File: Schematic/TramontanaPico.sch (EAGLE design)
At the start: 13 parts, among them U4 TEMT6000

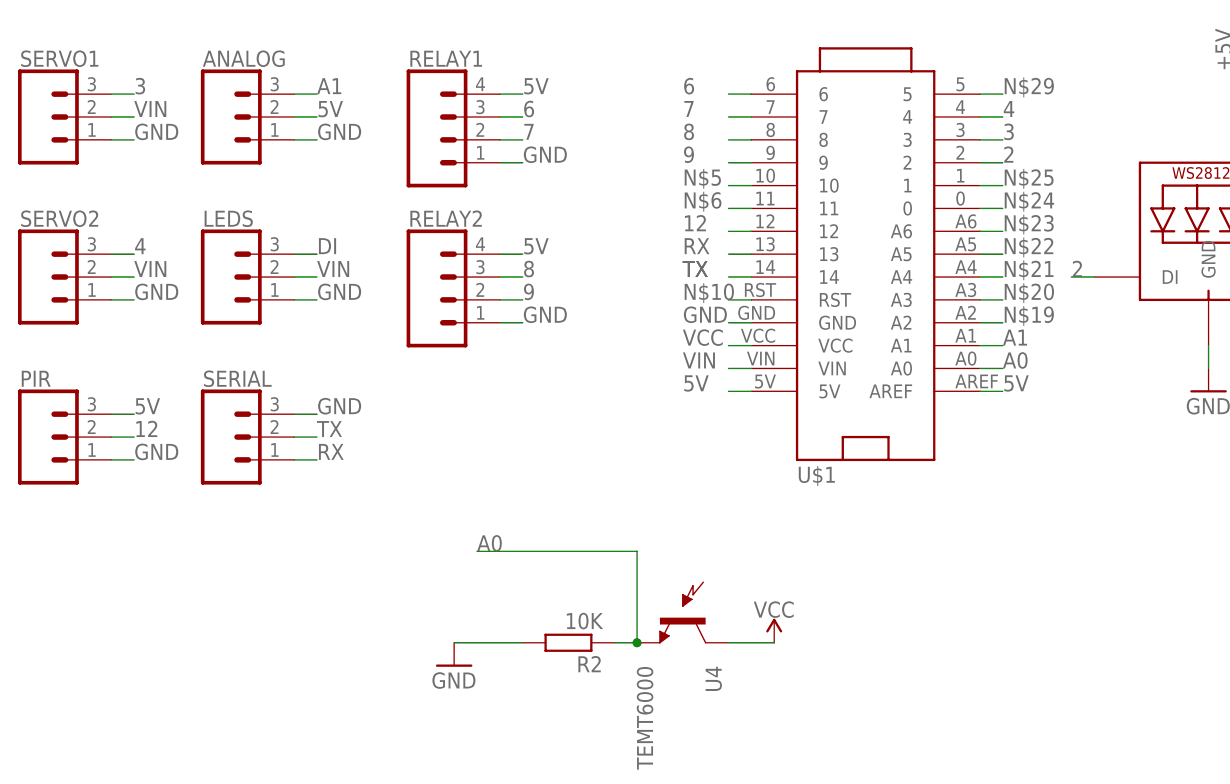
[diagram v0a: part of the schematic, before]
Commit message: added button
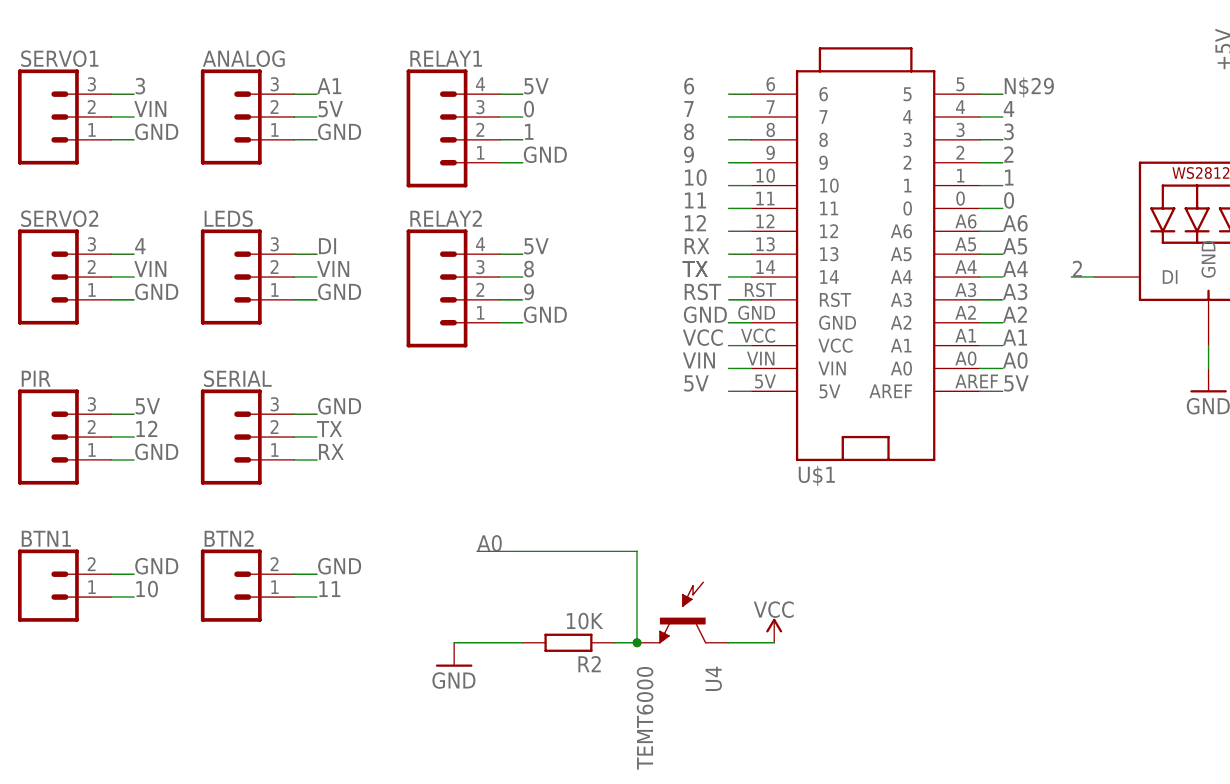
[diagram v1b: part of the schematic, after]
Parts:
- added BTN1, BTN2: (no value), SparkFun-Connectors:CONN_02LOCK
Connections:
- net N$10 renamed RST
- net N$19 renamed A2
- net N$20 renamed A3
- net N$21 renamed A4
- net N$22 renamed A5
- net N$23 renamed A6
- removed net N$24: U$1.0
- removed net N$25: U$1.1
- removed net N$5: U$1.10
- removed net N$6: U$1.11
- new net 0: RELAY1.3, U$1.0
- new net 1: RELAY1.2, U$1.1
- new net 10: BTN1.1, U$1.10
- new net 11: BTN2.1, U$1.11
- net 6: no longer RELAY1.3
- net 7: no longer RELAY1.2
- net GND: now also BTN1.2, BTN2.2
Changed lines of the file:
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@@
 <part name="U4" library="SparkFun" deviceset="TEMT6000" device=""/>
 <part name="SUPPLY1" library="SparkFun-PowerSymbols" deviceset="VCC" device=""/>
+<part name="BTN1" library="SparkFun-Connectors" deviceset="CONN_02" device="LOCK"/>
+<part name="BTN2" library="SparkFun-Connectors" deviceset="CONN_02" device="LOCK"/>
 </parts>
 <sheets>
@@
 <instance part="U4" gate="G$1" x="68.58" y="25.4" rot="R270"/>
 <instance part="SUPPLY1" gate="G$1" x="78.74" y="22.86"/>
+<instance part="BTN1" gate="G$1" x="-2.54" y="27.94"/>
+<instance part="BTN2" gate="G$1" x="17.78" y="27.94"/>
 </instances>
 <busses>
@@
 <wire x1="48.26" y1="58.42" x2="50.8" y2="58.42" width="0.1524" layer="91"/>
 <label x="50.8" y="58.42" size="1.778" layer="95"/>
+</segment>
+<segment>
+<pinref part="BTN1" gate="G$1" pin="2"/>
+<wire x1="5.08" y1="30.48" x2="7.62" y2="30.48" width="0.1524" layer="91"/>
+<label x="7.62" y="30.48" size="1.778" layer="95"/>
+</segment>
+<segment>
+<pinref part="BTN2" gate="G$1" pin="2"/>
+<wire x1="25.4" y1="30.48" x2="27.94" y2="30.48" width="0.1524" layer="91"/>
+<label x="27.94" y="30.48" size="1.778" layer="95"/>
 </segment>
 </net>
@@
 </segment>
 </net>
-<net name="N$5" class="0">
+<net name="10" class="0">
 <segment>
 <pinref part="U$1" gate="G$1" pin="10"/>
@@
 <label x="68.58" y="73.66" size="1.778" layer="95"/>
 </segment>
-</net>
-<net name="N$6" class="0">
+<segment>
+<pinref part="BTN1" gate="G$1" pin="1"/>
+<wire x1="5.08" y1="27.94" x2="7.62" y2="27.94" width="0.1524" layer="91"/>
+<label x="7.62" y="27.94" size="1.778" layer="95"/>
+</segment>
+</net>
+<net name="11" class="0">
 <segment>
 <pinref part="U$1" gate="G$1" pin="11"/>
@@
 <label x="68.58" y="71.12" size="1.778" layer="95"/>
 </segment>
-</net>
-<net name="N$10" class="0">
+<segment>
+<pinref part="BTN2" gate="G$1" pin="1"/>
+<wire x1="25.4" y1="27.94" x2="27.94" y2="27.94" width="0.1524" layer="91"/>
+<label x="27.94" y="27.94" size="1.778" layer="95"/>
+</segment>
+</net>
+<net name="RST" class="0">
 <segment>
 <pinref part="U$1" gate="G$1" pin="RST"/>
@@
 </segment>
 </net>
-<net name="N$19" class="0">
+<net name="A2" class="0">
 <segment>
 <pinref part="U$1" gate="G$1" pin="A2"/>
@@
 </segment>
 </net>
-<net name="N$20" class="0">
+<net name="A3" class="0">
 <segment>
 <pinref part="U$1" gate="G$1" pin="A3"/>
@@
 </segment>
 </net>
-<net name="N$21" class="0">
+<net name="A4" class="0">
 <segment>
 <pinref part="U$1" gate="G$1" pin="A4"/>
@@
 </segment>
 </net>
-<net name="N$22" class="0">
+<net name="A5" class="0">
 <segment>
 <pinref part="U$1" gate="G$1" pin="A5"/>
@@
 </segment>
 </net>
-<net name="N$23" class="0">
+<net name="A6" class="0">
 <segment>
 <pinref part="U$1" gate="G$1" pin="A6"/>
@@
 </segment>
 </net>
-<net name="N$24" class="0">
-<segment>
-<pinref part="U$1" gate="G$1" pin="0"/>
-<wire x1="101.6" y1="71.12" x2="104.14" y2="71.12" width="0.1524" layer="91"/>
-<label x="104.14" y="71.12" size="1.778" layer="95"/>
-</segment>
-</net>
-<net name="N$25" class="0">
+<net name="1" class="0">
 <segment>
 <pinref part="U$1" gate="G$1" pin="1"/>
 <wire x1="101.6" y1="73.66" x2="104.14" y2="73.66" width="0.1524" layer="91"/>
 <label x="104.14" y="73.66" size="1.778" layer="95"/>
+</segment>
+<segment>
+<pinref part="RELAY1" gate="G$1" pin="2"/>
+<wire x1="48.26" y1="78.74" x2="50.8" y2="78.74" width="0.1524" layer="91"/>
+<label x="50.8" y="78.74" size="1.778" layer="95"/>
 </segment>
 </net>
@@
 <net name="6" class="0">
 <segment>
+<pinref part="U$1" gate="G$1" pin="6"/>
+<wire x1="76.2" y1="83.82" x2="73.66" y2="83.82" width="0.1524" layer="91"/>
+<label x="68.58" y="83.82" size="1.778" layer="95"/>
+</segment>
+</net>
+<net name="7" class="0">
+<segment>
+<pinref part="U$1" gate="G$1" pin="7"/>
+<wire x1="76.2" y1="81.28" x2="73.66" y2="81.28" width="0.1524" layer="91"/>
+<label x="68.58" y="81.28" size="1.778" layer="95"/>
+</segment>
+</net>
+<net name="8" class="0">
+<segment>
+<pinref part="RELAY2" gate="G$1" pin="3"/>
+<wire x1="48.26" y1="63.5" x2="50.8" y2="63.5" width="0.1524" layer="91"/>
+<label x="50.8" y="63.5" size="1.778" layer="95"/>
+</segment>
+<segment>
+<pinref part="U$1" gate="G$1" pin="8"/>
+<wire x1="76.2" y1="78.74" x2="73.66" y2="78.74" width="0.1524" layer="91"/>
+<label x="68.58" y="78.74" size="1.778" layer="95"/>
+</segment>
+</net>
+<net name="9" class="0">
+<segment>
+<pinref part="RELAY2" gate="G$1" pin="2"/>
+<wire x1="48.26" y1="60.96" x2="50.8" y2="60.96" width="0.1524" layer="91"/>
+<label x="50.8" y="60.96" size="1.778" layer="95"/>
+</segment>
+<segment>
+<pinref part="U$1" gate="G$1" pin="9"/>
+<wire x1="76.2" y1="76.2" x2="73.66" y2="76.2" width="0.1524" layer="91"/>
+<label x="68.58" y="76.2" size="1.778" layer="95"/>
+</segment>
+</net>
+<net name="0" class="0">
+<segment>
 <pinref part="RELAY1" gate="G$1" pin="3"/>
 <wire x1="48.26" y1="81.28" x2="50.8" y2="81.28" width="0.1524" layer="91"/>
@@
 </segment>
 <segment>
-<pinref part="U$1" gate="G$1" pin="6"/>
-<wire x1="76.2" y1="83.82" x2="73.66" y2="83.82" width="0.1524" layer="91"/>
-<label x="68.58" y="83.82" size="1.778" layer="95"/>
-</segment>
-</net>
-<net name="7" class="0">
-<segment>
-<pinref part="RELAY1" gate="G$1" pin="2"/>
-<wire x1="48.26" y1="78.74" x2="50.8" y2="78.74" width="0.1524" layer="91"/>
-<label x="50.8" y="78.74" size="1.778" layer="95"/>
-</segment>
-<segment>
-<pinref part="U$1" gate="G$1" pin="7"/>
-<wire x1="76.2" y1="81.28" x2="73.66" y2="81.28" width="0.1524" layer="91"/>
-<label x="68.58" y="81.28" size="1.778" layer="95"/>
-</segment>
-</net>
-<net name="8" class="0">
-<segment>
-<pinref part="RELAY2" gate="G$1" pin="3"/>
-<wire x1="48.26" y1="63.5" x2="50.8" y2="63.5" width="0.1524" layer="91"/>
-<label x="50.8" y="63.5" size="1.778" layer="95"/>
-</segment>
-<segment>
-<pinref part="U$1" gate="G$1" pin="8"/>
-<wire x1="76.2" y1="78.74" x2="73.66" y2="78.74" width="0.1524" layer="91"/>
-<label x="68.58" y="78.74" size="1.778" layer="95"/>
-</segment>
-</net>
-<net name="9" class="0">
-<segment>
-<pinref part="RELAY2" gate="G$1" pin="2"/>
-<wire x1="48.26" y1="60.96" x2="50.8" y2="60.96" width="0.1524" layer="91"/>
-<label x="50.8" y="60.96" size="1.778" layer="95"/>
-</segment>
-<segment>
-<pinref part="U$1" gate="G$1" pin="9"/>
-<wire x1="76.2" y1="76.2" x2="73.66" y2="76.2" width="0.1524" layer="91"/>
-<label x="68.58" y="76.2" size="1.778" layer="95"/>
-</segment>
-</net>
+<pinref part="U$1" gate="G$1" pin="0"/>
+<wire x1="101.6" y1="71.12" x2="104.14" y2="71.12" width="0.1524" layer="91"/>
+<label x="104.14" y="71.12" size="1.778" layer="95"/>
+</segment>
+</net>

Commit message: improvements
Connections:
- net N$29 renamed 5
- removed net N$14: U$1.5V
- new net AREF: U$1.AREF
- net 5V: now also C4.1, LED1.VDD, LEDS.2, SERVO1.2, SERVO2.2, U$1.5V, U4.C1; no longer U$1.AREF
- net VCC: no longer U4.C1
- net VIN: no longer C4.1, LED1.VDD, LEDS.2, SERVO1.2, SERVO2.2

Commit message: pier's version
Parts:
- added HTTP: FRAME_DINA4_L, dp_devices:FRAME_DINA4_L
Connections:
- removed net 5V: ANALOG.2, C4.1, LED1.VDD, LEDS.2, PIR.3, RELAY1.4, RELAY2.4, SERVO1.2, SERVO2.2, U$1.5V, U4.C1
- removed net VCC: U$1.VCC
- removed net VIN: U$1.VIN
- new net 5V_EXT: U$1.5V
- new net VCC_3V3: ANALOG.2, U$1.VCC
- new net VIN_5V: C4.1, LED1.VDD, LEDS.2, PIR.3, RELAY1.4, RELAY2.4, SERVO1.2, SERVO2.2, U$1.VIN, U4.C1
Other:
- moved on the sheet: ANALOG, BTN1, BTN2, C4, LEDS, PIR, R2, RELAY1, RELAY2, SERIAL, SERVO1, SERVO2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
